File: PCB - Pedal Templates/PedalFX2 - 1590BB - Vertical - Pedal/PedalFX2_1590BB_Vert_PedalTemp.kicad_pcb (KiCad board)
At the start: 2 copper layers, 89 x 44.7 mm, 12 parts, among them J1 Conn_01x04_Female, T1 ACJS-MHDR, T2 ACJS-MHDR, T3 54-00129

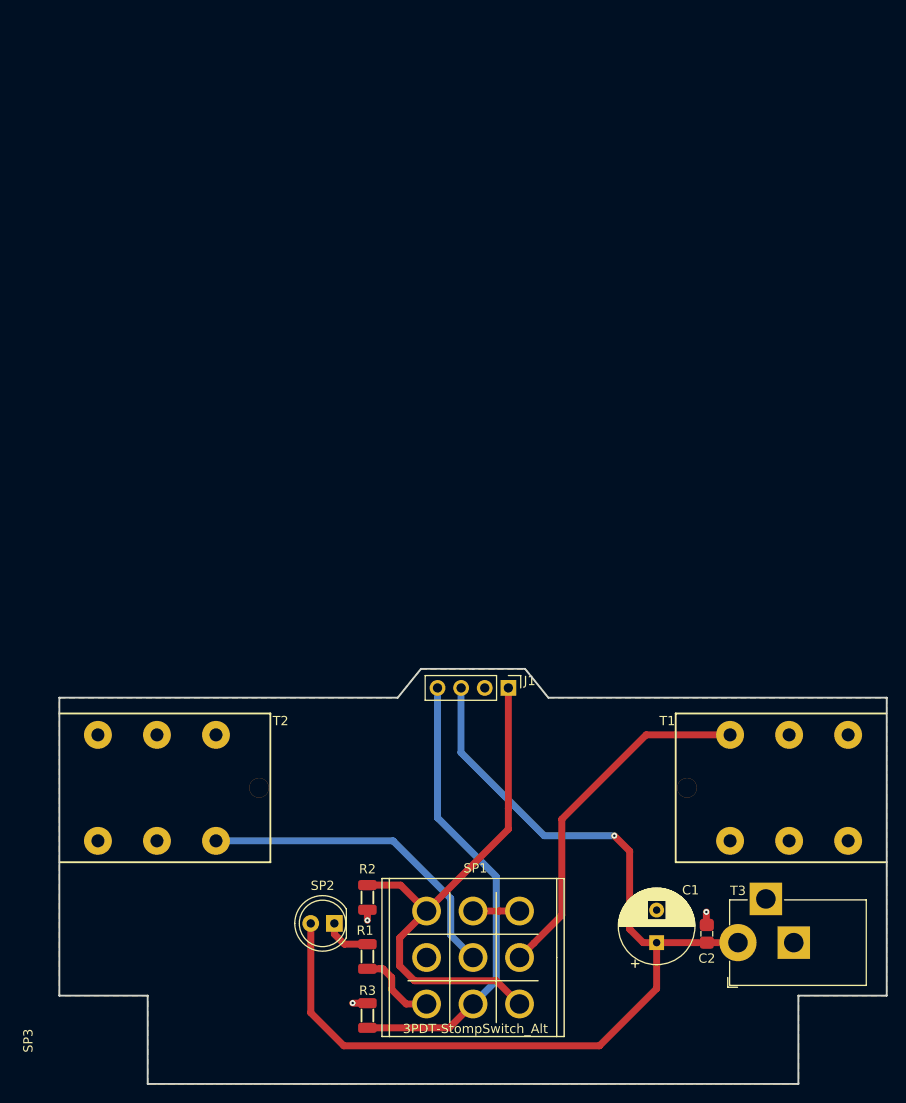
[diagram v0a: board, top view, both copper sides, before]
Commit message: Templates
Added pedal templates for each size of PedalFX2
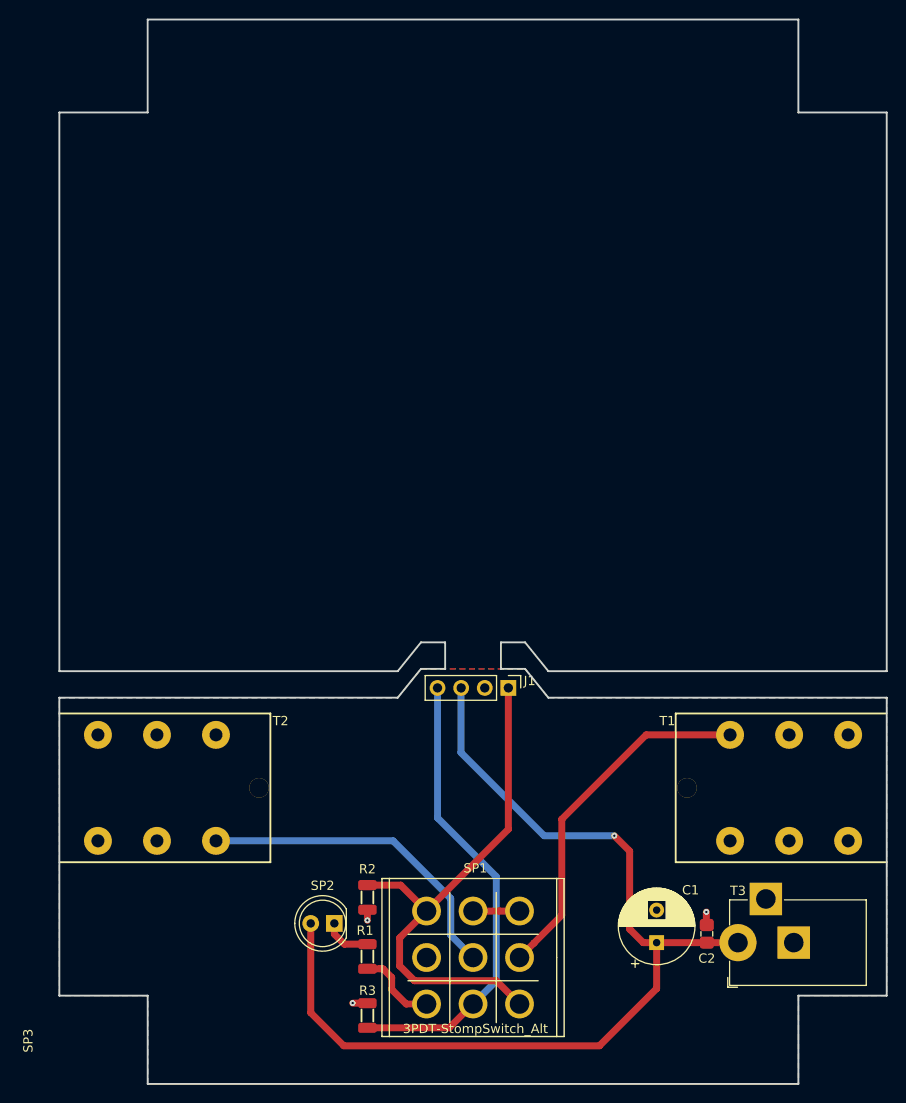
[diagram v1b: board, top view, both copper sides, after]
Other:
- board size 89 x 44.7 mm -> 89 x 114.5 mm
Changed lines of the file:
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@@
   (general
     (thickness 1.6)
-    (drawings 25)
+    (drawings 40)
     (tracks 61)
     (zones 0)
@@
     )
   )
+  (gr_line (start 193 48) (end 193 38) (layer Edge.Cuts) (width 0.2))
+  (gr_line (start 202.5 48) (end 193 48) (layer Edge.Cuts) (width 0.2))
+  (gr_line (start 123 38) (end 193 38) (layer Edge.Cuts) (width 0.2))
+  (gr_line (start 123 48) (end 123 38) (layer Edge.Cuts) (width 0.2))
+  (gr_line (start 113.5 48) (end 123 48) (layer Edge.Cuts) (width 0.2))
+  (gr_line (start 113.5 48) (end 113.5 108.1) (layer Edge.Cuts) (width 0.2))
+  (gr_line (start 202.5 48) (end 202.5 108.1) (layer Edge.Cuts) (width 0.2))
+  (gr_line (start 163.6 105) (end 166.1 108.1) (layer Edge.Cuts) (width 0.2))
+  (gr_line (start 161 105) (end 163.6 105) (layer Edge.Cuts) (width 0.2))
+  (gr_line (start 166.1 108.1) (end 202.5 108.1) (layer Edge.Cuts) (width 0.2))
+  (gr_line (start 149.9 108.1) (end 152.4 105) (layer Edge.Cuts) (width 0.2))
+  (gr_line (start 155 105) (end 152.4 105) (layer Edge.Cuts) (width 0.2))
+  (gr_line (start 149.9 108.1) (end 113.5 108.1) (layer Edge.Cuts) (width 0.2))
+  (gr_line (start 155 107.85) (end 155 105) (layer Edge.Cuts) (width 0.2))
+  (gr_line (start 161 107.85) (end 161 105) (layer Edge.Cuts) (width 0.2))
   (gr_line (start 166 111.15) (end 202.3 111.15) (layer Margin) (width 0.15))
   (gr_line (start 202.3 142.8) (end 202.3 111.15) (layer Margin) (width 0.15))
@@
   (gr_line (start 152.5 108.05) (end 163.5 108.05) (layer Margin) (width 0.15))
   (gr_line (start 150 111.15) (end 152.5 108.05) (layer Margin) (width 0.15))
-  (gr_line (start 158 107.85) (end 152.4 107.85) (layer Edge.Cuts) (width 0.2))
-  (gr_line (start 158 107.85) (end 163.6 107.85) (layer Edge.Cuts) (width 0.2))
+  (gr_line (start 155 107.85) (end 152.4 107.85) (layer Edge.Cuts) (width 0.2))
+  (gr_line (start 161 107.85) (end 163.6 107.85) (layer Edge.Cuts) (width 0.2))
   (gr_line (start 149.9 110.95) (end 152.4 107.85) (layer Edge.Cuts) (width 0.2))
   (gr_line (start 163.6 107.85) (end 166.1 110.95) (layer Edge.Cuts) (width 0.2))
